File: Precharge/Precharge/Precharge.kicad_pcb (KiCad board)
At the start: 2 copper layers, 133 x 98 mm, 118 parts, among them J1 MicroFit, K1 OMRON-G2RL-24, K2 G7L-2A-X-L, Q1 2N7002, Q2 MMBT3906, Q3 2N7002, U1 TJA1051T-3, U10 LM393, U11 4N35, U2 SPAN02A-12, U3 Teensy4.0, U4 LM1117-5.0, U5 4N35, U6 4N35, U7 LM331, U8 LM331, U9 LM2904

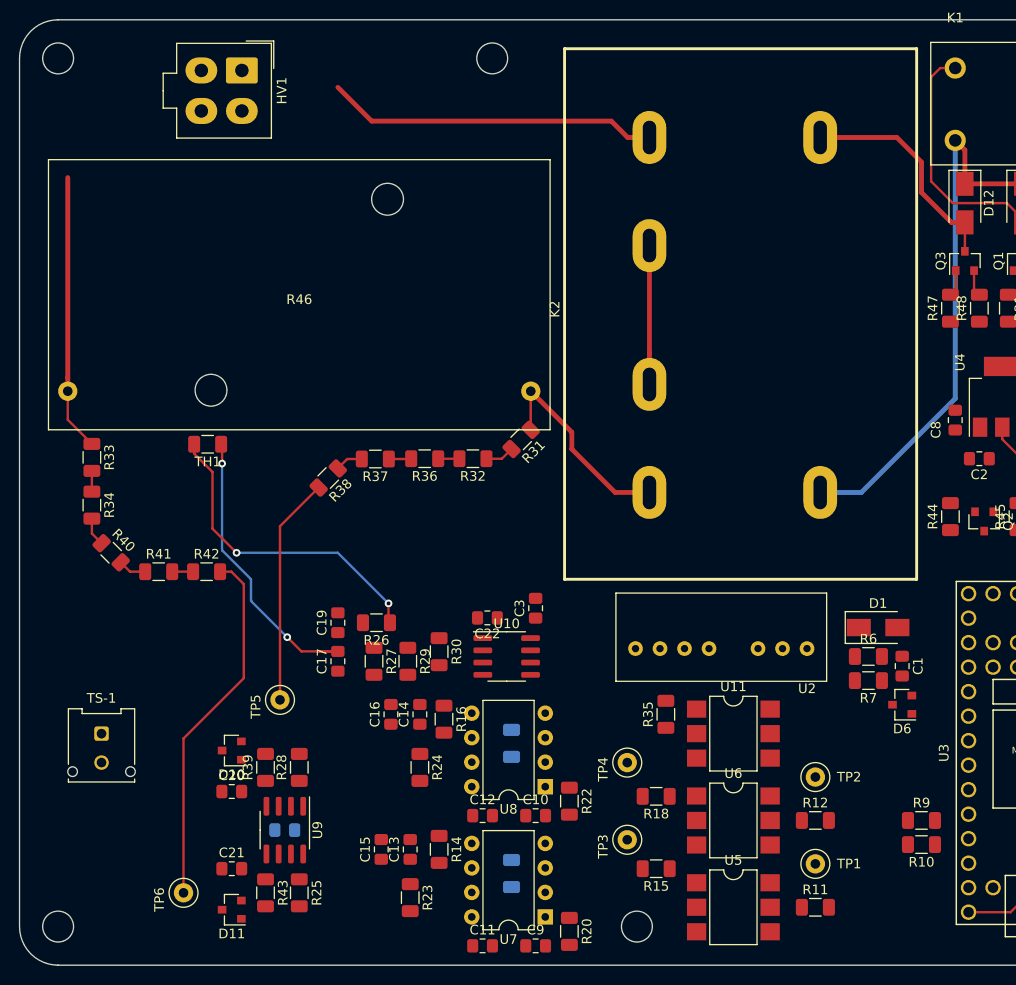
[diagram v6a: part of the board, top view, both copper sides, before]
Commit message: :pencil2: manual route the critical paths
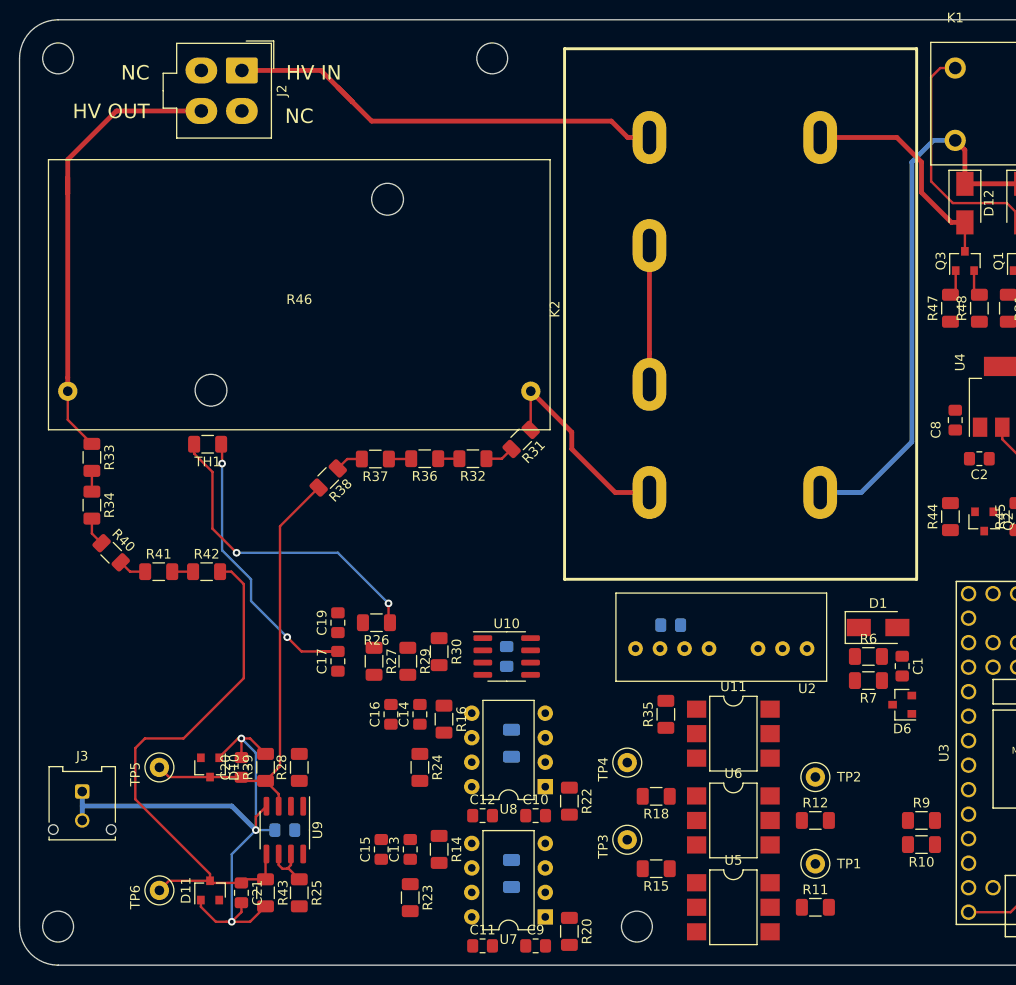
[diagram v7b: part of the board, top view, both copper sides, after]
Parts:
- C22, C3: moved to B.Cu
- moved TP5 14.3 mm to (82.5, 128.0)
- moved C3 14.1 mm to (135.5, 113.2), turned to 0 degrees
- moved J3 6.32 mm to (74.5, 130.5)
- moved C22 4.47 mm to (118.5, 116.5), turned to 270 degrees
- moved D11 3.01 mm to (87.8, 140.8), turned to 90 degrees
- moved D10 2.85 mm to (87.8, 128.0), turned to 270 degrees
- moved C20 2.69 mm to (91.0, 128.0), turned to 90 degrees
- moved C21 2.69 mm to (91.0, 141.0), turned to 270 degrees
- moved TP6 2.51 mm to (82.5, 140.8)
- renumbered HV1 to J2, TS-1 to J3
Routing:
- net GNDS: track 0.00 -> 67.0 mm, vias 0 -> 3
- net Net-(C20-Pad1): track 23.7 -> 47.5 mm
- net Net-(C21-Pad1): track 37.6 -> 58.3 mm
- net /VinTS: track 28.6 -> 48.1 mm
- net Net-(J2-Pad1): track 34.5 -> 47.3 mm
- net Net-(R25-Pad1): track 0.00 -> 5.57 mm
- net +12V: track 114.3 -> 115.6 mm
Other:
- board text added: "HV IN"
- board text added: "HV OUT"
- board text added: "NC"

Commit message: :hammer: complete routing
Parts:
- added R49: 0, Resistor_SMD:R_1206_3216Metric, B.Cu at (81.0, 132.0)
- moved C3 1.00 mm to (135.5, 112.2)
- moved TH1 0.50 mm to (88.0, 94.5), turned to 0 degrees
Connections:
- J3 pad 1: GNDS -> /TS-
- J3 pad 2: GNDS -> /TS-
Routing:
- net GLV-: track 7.93 -> 319.2 mm, vias 0 -> 1
- net GNDS: track 67.0 -> 282.4 mm
- net +12P: track 33.1 -> 200.1 mm
- net +3V3: track 0.00 -> 88.8 mm
- net +12V: track 115.6 -> 188.0 mm
- net /PDOC_OK: track 0.00 -> 68.3 mm, vias 0 -> 1
- net GLV+: track 43.8 -> 92.4 mm, vias 0 -> 1
- net /SHTDN_CTRL: track 0.00 -> 38.7 mm, vias 0 -> 1
- net Net-(Q2-Pad1): track 0.00 -> 38.6 mm
- net /Fts: track 0.00 -> 38.3 mm
- net /PRECHG: track 0.00 -> 37.1 mm, vias 0 -> 1
- net Net-(C15-Pad1): track 0.00 -> 36.0 mm
- net +5V: track 66.0 -> 99.4 mm
- net Net-(C16-Pad1): track 0.00 -> 33.3 mm
- net /Faccu: track 0.00 -> 31.8 mm
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- added copper zone on B.Cu, net /TS-
- added copper zone on F.Cu, net /TS-
